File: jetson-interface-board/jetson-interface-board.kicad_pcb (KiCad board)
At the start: 2 copper layers, 47 x 23 mm, 36 parts, among them J1 Conn_01x04, J2 Conn_01x04, J3 USB_C_Receptacle_USB2.0, J4 Conn_01x04, J5 Conn_01x18, SW1 SW_Push, U1 MCP2562-E-MF, U2 FT234XD, U3 XC8111AA01MR-G, U4 XC8111AA01MR-G

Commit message: jetson-rtc ビア以外完成
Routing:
- net +5V: track 44.8 -> 44.1 mm
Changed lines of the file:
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@@
 	)
 	(segment
-		(start 34.3 19.2)
-		(end 32.5 21)
-		(width 0.6)
+		(start 48.55 19.65)
+		(end 48.1 19.2)
+		(width 0.2)
 		(layer "F.Cu")
 		(net 3)
@@
 	)
 	(segment
-		(start 47.5125 21.65)
-		(end 47.6 21.7375)
-		(width 0.6)
-		(layer "F.Cu")
-		(net 3)
-	)
-	(segment
-		(start 32.5 21)
-		(end 32.5 21.275)
-		(width 0.6)
+		(start 47.6 21.7375)
+		(end 47.925 22.0625)
+		(width 0.2)
 		(layer "F.Cu")
 		(net 3)
@@
 	)
 	(segment
-		(start 34.575 19.2)
-		(end 48.1 19.2)
-		(width 0.6)
+		(start 48.593751 19.65)
+		(end 49.243751 20.3)
+		(width 0.2)
+		(layer "F.Cu")
+		(net 3)
+	)
+	(segment
+		(start 45.8375 21.65)
+		(end 45.925 21.7375)
+		(width 0.2)
 		(layer "F.Cu")
 		(net 3)
@@
 	)
 	(segment
-		(start 45.8375 21.65)
-		(end 47.5125 21.65)
-		(width 0.6)
+		(start 48.1 19.2)
+		(end 34.575 19.2)
+		(width 0.2)
 		(layer "F.Cu")
 		(net 3)
 	)
 	(segment
-		(start 47.6 21.7375)
-		(end 48.875 21.7375)
-		(width 0.6)
+		(start 49.243751 22.018749)
+		(end 49.243751 20.3)
+		(width 0.2)
 		(layer "F.Cu")
 		(net 3)
@@
 	)
 	(segment
-		(start 48.875 21.7375)
+		(start 47.925 22.0625)
 		(end 49.2 22.0625)
-		(width 0.6)
+		(width 0.2)
+		(layer "F.Cu")
+		(net 3)
+	)
+	(segment
+		(start 49.2 22.0625)
+		(end 49.243751 22.018749)
+		(width 0.2)
 		(layer "F.Cu")
 		(net 3)
@@
 	(segment
 		(start 48.55 19.65)
-		(end 48.1 19.2)
-		(width 0.6)
-		(layer "F.Cu")
-		(net 3)
-	)
-	(segment
-		(start 49.2 22.0625)
-		(end 49.2 20.343751)
-		(width 0.6)
-		(layer "F.Cu")
-		(net 3)
-	)
-	(segment
-		(start 34.575 19.2)
-		(end 34.3 19.2)
-		(width 0.6)
+		(end 48.593751 19.65)
+		(width 0.2)
 		(layer "F.Cu")
 		(net 3)
@@
 	)
 	(segment
-		(start 49.2 20.3)
-		(end 48.1 19.2)
-		(width 0.6)
+		(start 34.575 19.2)
+		(end 32.5 21.275)
+		(width 0.2)
 		(layer "F.Cu")
 		(net 3)
+	)
+	(segment
+		(start 45.925 21.7375)
+		(end 47.6 21.7375)
+		(width 0.2)
+		(layer "F.Cu")
+		(net 3)

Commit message: ビア打ち、シルク、ガーバ生成
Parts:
- added G***: LOGO, LOGO, F.Cu at (20.4, 25.2)
- added REF**: MountingHole_3.2mm_M3, MountingHole:MountingHole_3.2mm_M3, F.Cu at (19.0, 34.0)
- added REF**: MountingHole_3.2mm_M3, MountingHole:MountingHole_3.2mm_M3, F.Cu at (19.0, 19.0)
- added REF**: MountingHole_3.2mm_M3, MountingHole:MountingHole_3.2mm_M3, F.Cu at (74.0, 19.0)
- added REF**: MountingHole_3.2mm_M3, MountingHole:MountingHole_3.2mm_M3, F.Cu at (74.0, 34.0)
- moved J5 8.00 mm to (68.0, 16.4)
- moved C1 8.00 mm to (27.6, 22.1)
- moved C2 8.00 mm to (29.2, 18.9)
- moved C3 8.00 mm to (63.3, 34.7)
- moved C4 8.00 mm to (65.8, 35.5)
- moved C5 8.00 mm to (58.1, 26.1)
- moved C6 8.00 mm to (58.1, 20.3)
- moved C7 8.00 mm to (55.3, 26.5)
- moved C8 8.00 mm to (49.8, 22.6)
- moved C9 8.00 mm to (55.6, 22.6)
- moved D1 8.00 mm to (68.1, 28.1)
- moved D2 8.00 mm to (68.1, 22.8)
- moved D3 8.00 mm to (68.1, 26.0)
- moved D4 8.00 mm to (68.1, 21.2)
- moved D5 8.00 mm to (68.1, 19.6)
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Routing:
- net GNDD: vias 3 -> 75
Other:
- board size 47 x 23 mm -> 63 x 23 mm
- board text added: "H 5 L G"
- board text added: "create by ikeda"
- board text added: "jetson-interface-board"
- board text added: "version1.0"

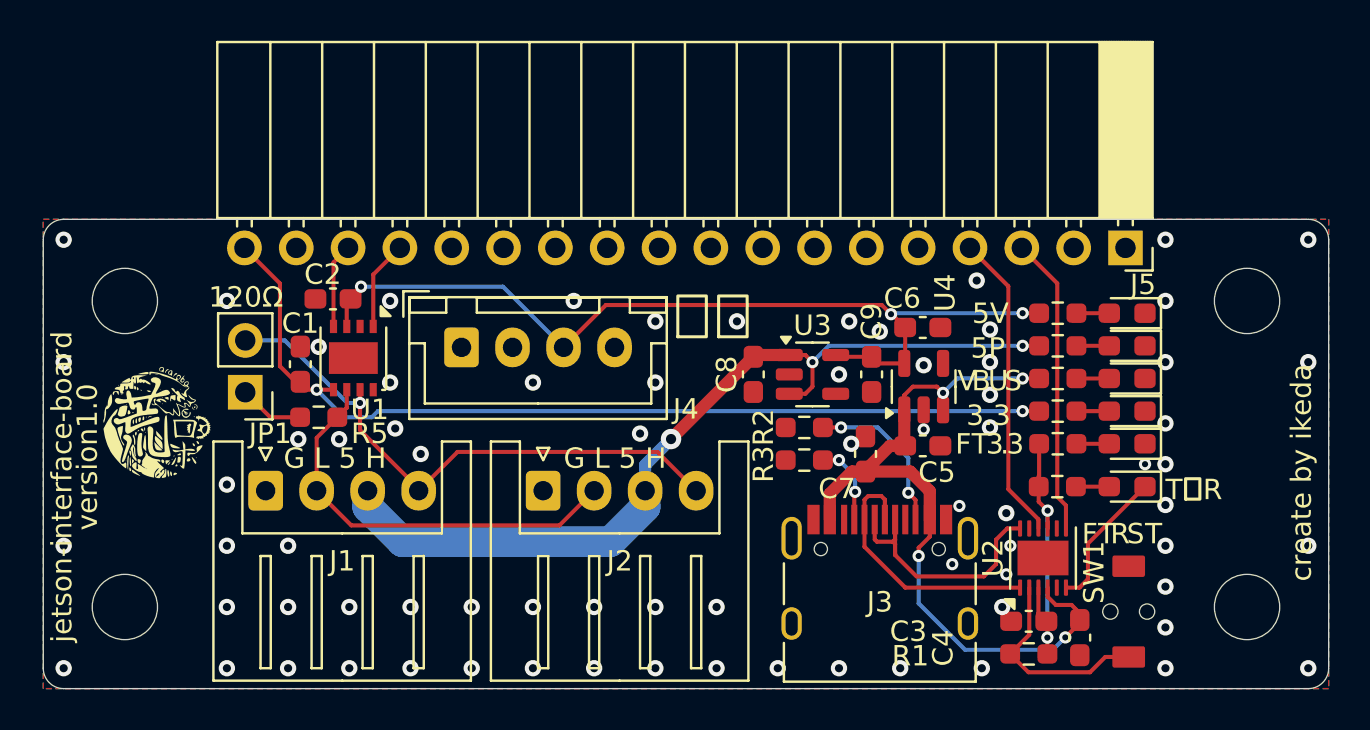
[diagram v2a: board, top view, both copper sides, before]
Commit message: feat:インジケータとスイッチ変更および再配線・再配置
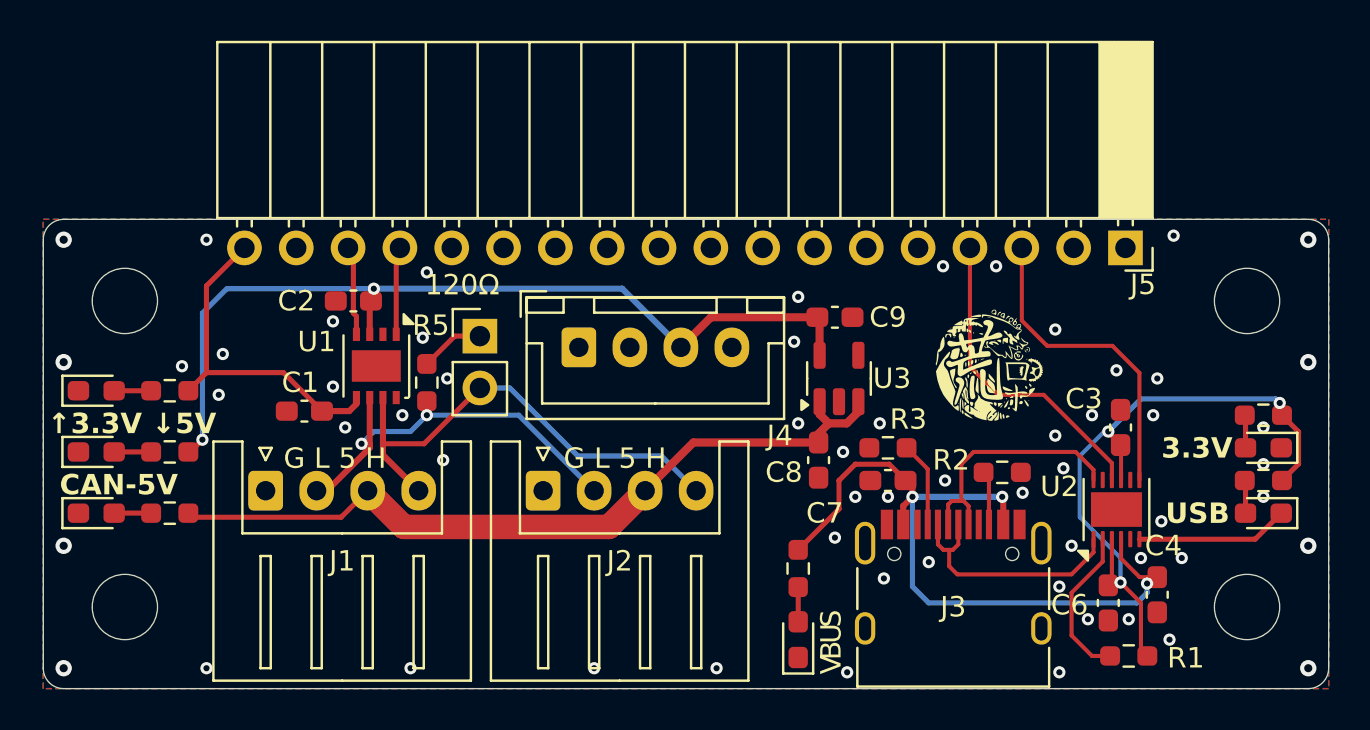
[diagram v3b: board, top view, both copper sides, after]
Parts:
- removed C5: 1uf, Capacitor_SMD:C_0603_1608Metric_Pad1.08x0.95mm_HandSolder
- removed SW1: SW_Push, 0Ikedalibrary:switch_TVAF06-A020B-R
- removed U4: XC8111AA01MR-G, Package_TO_SOT_SMD:SOT-23-5
- C6: value 1uf -> 4.7uf
- moved D4 51.2 mm to (17.6, 29.4), turned to 0 degrees
- moved D5 51.0 mm to (17.6, 26.4), turned to 0 degrees
- moved D6 50.5 mm to (17.6, 23.4), turned to 0 degrees
- moved R8 44.3 mm to (21.2, 29.4), turned to 0 degrees
- moved R9 44.1 mm to (21.2, 26.4), turned to 0 degrees
- moved R10 43.5 mm to (21.2, 23.4), turned to 0 degrees
- moved G*** 40.9 mm to (61.2, 22.4)
- moved D2 20.6 mm to (52.0, 35.6), turned to 90 degrees
- moved C6 16.3 mm to (67.2, 33.8), turned to -90 degrees
- moved R6 15.8 mm to (52.0, 32.1), turned to 90 degrees
- moved JP1 11.8 mm to (36.4, 20.7), turned to 0 degrees
- moved C3 10.5 mm to (67.8, 25.2), turned to 90 degrees
- moved R7 10.2 mm to (74.8, 24.6), turned to 0 degrees
- moved R4 10.1 mm to (74.8, 27.8), turned to 0 degrees
- moved R2 9.95 mm to (62.0, 27.4), turned to 0 degrees
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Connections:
- C6 pad 1: +5V -> 3.3V_FT
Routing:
- net +3.3V: track 45.7 -> 16.7 mm, vias 2 -> 0
- net 3.3V_FT: track 14.0 -> 32.9 mm, vias 2 -> 3
- net Net-(J3-CC2): track 7.97 -> 2.66 mm, vias 2 -> 0
- net CANH: track 28.2 -> 23.9 mm, vias 1 -> 0
- net +5VP: track 42.4 -> 38.5 mm, vias 3 -> 0
- net Net-(U2-~{RESET}): track 10.1 -> 7.66 mm
- net VBUS: track 37.9 -> 36.4 mm, vias 4 -> 3
- net USBD+: track 13.7 -> 12.4 mm
- net UART_RX: track 14.6 -> 15.6 mm
- net USBD-: track 12.9 -> 12.3 mm
- net Net-(D1-K): track 6.94 -> 7.48 mm
- net +5V: track 44.1 -> 43.8 mm, vias 3 -> 2
- net Net-(J3-CC1): track 4.05 -> 4.18 mm, vias 2 -> 0
- net CANL: track 20.6 -> 20.5 mm, vias 0 -> 2
- net GNDD: vias 75 -> 59
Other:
- board text added: "3.3V"
- board text added: "CAN-5V"
- board text added: "USB"
- board text added: "create by Ikeda and Aiba"
- board text added: "↑3.3V ↓5V"
- board text removed: "."
- board text removed: "3"
- board text removed: "3.3"
- board text removed: "5P"
- board text removed: "5V"
- board text removed: "F"
- board text removed: "R"
- board text removed: "T"
- board text removed: "T・R"
- board text removed: "create by ikeda"
- board text removed: "version1.0"
- board text removed: "電源"
